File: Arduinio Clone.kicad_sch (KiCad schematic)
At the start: 0 parts

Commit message: Added child connectors schematic and symbols
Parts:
- added BT?: Battery, symbol Device:Battery
- added C?: C_Polarized, symbol Device:C_Polarized
- added C? (x2): C, symbol Device:C
- added D?: LED, symbol Device:LED
- added R? (x2): R, symbol Device:R
- added U?: 24LC1025, symbol Memory_EEPROM:24LC1025
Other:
- added sheet Connectors (Connectors.kicad_sch)
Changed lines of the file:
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@@
     (comment 1 "Designe by Giddie")
+  )
+  (symbol (lib_id "Device:LED") (at 93.98 90.17 0) (unit 1)
+    (in_bom yes) (on_board yes) (fields_autoplaced)
+    (property "Reference" "D?" (id 0) (at 92.3925 83.82 0))
+    (property "Value" "LED" (id 1) (at 92.3925 86.36 0))
+    (property "Footprint" "" (id 2) (at 93.98 90.17 0)
+      (effects (font (size 1.27 1.27)) hide)
+    )
+    (property "Datasheet" "~" (id 3) (at 93.98 90.17 0)
+      (effects (font (size 1.27 1.27)) hide)
+    )
+    (pin "1")
+    (pin "2")
+  )
+  (symbol (lib_id "Memory_EEPROM:24LC1025") (at 144.78 82.55 0) (unit 1)
+    (in_bom yes) (on_board yes) (fields_autoplaced)
+    (property "Reference" "U?" (id 0) (at 146.7994 72.39 0)
+      (effects (font (size 1.27 1.27)) (justify left))
+    )
+    (property "Value" "24LC1025" (id 1) (at 146.7994 74.93 0)
+      (effects (font (size 1.27 1.27)) (justify left))
+    )
+    (property "Footprint" "" (id 2) (at 144.78 82.55 0)
+      (effects (font (size 1.27 1.27)) hide)
+    )
+    (property "Datasheet" "http://ww1.microchip.com/downloads/en/DeviceDoc/21941B.pdf" (id 3) (at 144.78 82.55 0)
+      (effects (font (size 1.27 1.27)) hide)
+    )
+    (pin "1")
+    (pin "2")
+    (pin "3")
+    (pin "4")
+    (pin "5")
+    (pin "6")
+    (pin "7")
+    (pin "8")
+  )
+  (symbol (lib_id "Device:C_Polarized") (at 128.27 54.61 0) (unit 1)
+    (in_bom yes) (on_board yes) (fields_autoplaced)
+    (property "Reference" "C?" (id 0) (at 132.08 52.4509 0)
+      (effects (font (size 1.27 1.27)) (justify left))
+    )
+    (property "Value" "C_Polarized" (id 1) (at 132.08 54.9909 0)
+      (effects (font (size 1.27 1.27)) (justify left))
+    )
+    (property "Footprint" "" (id 2) (at 129.2352 58.42 0)
+      (effects (font (size 1.27 1.27)) hide)
+    )
+    (property "Datasheet" "~" (id 3) (at 128.27 54.61 0)
+      (effects (font (size 1.27 1.27)) hide)
+    )
+    (pin "1")
+    (pin "2")
+  )
+  (symbol (lib_id "Device:C") (at 91.44 55.88 0) (unit 1)
+    (in_bom yes) (on_board yes) (fields_autoplaced)
+    (property "Reference" "C?" (id 0) (at 95.25 54.6099 0)
+      (effects (font (size 1.27 1.27)) (justify left))
+    )
+    (property "Value" "C" (id 1) (at 95.25 57.1499 0)
+      (effects (font (size 1.27 1.27)) (justify left))
+    )
+    (property "Footprint" "" (id 2) (at 92.4052 59.69 0)
+      (effects (font (size 1.27 1.27)) hide)
+    )
+    (property "Datasheet" "~" (id 3) (at 91.44 55.88 0)
+      (effects (font (size 1.27 1.27)) hide)
+    )
+    (pin "1")
+    (pin "2")
+  )
+  (symbol (lib_id "Device:R") (at 123.19 87.63 0) (unit 1)
+    (in_bom yes) (on_board yes) (fields_autoplaced)
+    (property "Reference" "R?" (id 0) (at 125.73 86.3599 0)
+      (effects (font (size 1.27 1.27)) (justify left))
+    )
+    (property "Value" "R" (id 1) (at 125.73 88.8999 0)
+      (effects (font (size 1.27 1.27)) (justify left))
+    )
+    (property "Footprint" "" (id 2) (at 121.412 87.63 90)
+      (effects (font (size 1.27 1.27)) hide)
+    )
+    (property "Datasheet" "~" (id 3) (at 123.19 87.63 0)
+      (effects (font (size 1.27 1.27)) hide)
+    )
+    (pin "1")
+    (pin "2")
+  )
+  (symbol (lib_id "Device:Battery") (at 63.5 53.34 0) (unit 1)
+    (in_bom yes) (on_board yes) (fields_autoplaced)
+    (property "Reference" "BT?" (id 0) (at 67.31 51.6889 0)
+      (effects (font (size 1.27 1.27)) (justify left))
+    )
+    (property "Value" "Battery" (id 1) (at 67.31 54.2289 0)
+      (effects (font (size 1.27 1.27)) (justify left))
+    )
+    (property "Footprint" "" (id 2) (at 63.5 51.816 90)
+      (effects (font (size 1.27 1.27)) hide)
+    )
+    (property "Datasheet" "~" (id 3) (at 63.5 51.816 90)
+      (effects (font (size 1.27 1.27)) hide)
+    )
+    (pin "1")
+    (pin "2")
+  )
+  (symbol (lib_id "Device:R") (at 111.76 71.12 0) (unit 1)
+    (in_bom yes) (on_board yes) (fields_autoplaced)
+    (property "Reference" "R?" (id 0) (at 114.3 69.8499 0)
+      (effects (font (size 1.27 1.27)) (justify left))
+    )
+    (property "Value" "R" (id 1) (at 114.3 72.3899 0)
+      (effects (font (size 1.27 1.27)) (justify left))
+    )
+    (property "Footprint" "" (id 2) (at 109.982 71.12 90)
+      (effects (font (size 1.27 1.27)) hide)
+    )
+    (property "Datasheet" "~" (id 3) (at 111.76 71.12 0)
+      (effects (font (size 1.27 1.27)) hide)
+    )
+    (pin "1")
+    (pin "2")
+  )
+  (symbol (lib_id "Device:C") (at 110.49 53.34 0) (unit 1)
+    (in_bom yes) (on_board yes) (fields_autoplaced)
+    (property "Reference" "C?" (id 0) (at 114.3 52.0699 0)
+      (effects (font (size 1.27 1.27)) (justify left))
+    )
+    (property "Value" "C" (id 1) (at 114.3 54.6099 0)
+      (effects (font (size 1.27 1.27)) (justify left))
+    )
+    (property "Footprint" "" (id 2) (at 111.4552 57.15 0)
+      (effects (font (size 1.27 1.27)) hide)
+    )
+    (property "Datasheet" "~" (id 3) (at 110.49 53.34 0)
+      (effects (font (size 1.27 1.27)) hide)
+    )
+    (pin "1")
+    (pin "2")
+  )
+  (sheet (at 68.58 110.49) (size 57.15 49.53) (fields_autoplaced)
+    (stroke (width 0.1524) (type solid) (color 0 0 0 0))
+    (fill (color 0 0 0 0.0000))
+    (property "Sheet name" "Connectors" (id 0) (at 68.58 109.7784 0)
+      (effects (font (size 1.27 1.27)) (justify left bottom))
+    )
+    (property "Sheet file" "Connectors.kicad_sch" (id 1) (at 68.58 160.6046 0)
+      (effects (font (size 1.27 1.27)) (justify left top))
+    )
   )
   (sheet_instances
     (path "/" (page "1"))
+    (path "/99dcd93f-6742-4b81-a071-043df0a32b88" (page "2"))
+  )
+  (symbol_instances
+    (path "/cb99d522-d98f-4f2e-af24-39a642a2262c"
+      (reference "BT?") (unit 1) (value "Battery") (footprint "")
+    )
+    (path "/47ac9772-3d12-4e4c-be34-49c86c4d11b8"
+      (reference "C?") (unit 1) (value "C_Polarized") (footprint "")
+    )
+    (path "/a0a7411e-2ace-431e-9190-e1efd84cfa19"
+      (reference "C?") (unit 1) (value "C") (footprint "")
+    )
+    (path "/f4cd744f-86c3-401e-9dc4-f3966535b983"
+      (reference "C?") (unit 1) (value "C") (footprint "")
+    )
+    (path "/10f0ad0a-5347-4cd8-9e8b-b551768717e1"
+      (reference "D?") (unit 1) (value "LED") (footprint "")
+    )
+    (path "/99dcd93f-6742-4b81-a071-043df0a32b88/627a6bb9-dcd8-4955-91b8-8ac1c7ba0267"
+      (reference "J?") (unit 1) (value "Conn_01x09") (footprint "")
+    )
+    (path "/99dcd93f-6742-4b81-a071-043df0a32b88/70a1e371-96bd-43fc-8ac7-1645345d3e46"
+      (reference "J?") (unit 1) (value "Conn_02x03_Odd_Even") (footprint "")
+    )
+    (path "/99dcd93f-6742-4b81-a071-043df0a32b88/b8095f78-b7cb-4edb-8f3b-82dfbdf61388"
+      (reference "J?") (unit 1) (value "Conn_01x04") (footprint "")
+    )
+    (path "/99dcd93f-6742-4b81-a071-043df0a32b88/dd61ea61-ee00-483a-9cf3-44579a861992"
+      (reference "J?") (unit 1) (value "Conn_01x04") (footprint "")
+    )
+    (path "/a514a1f9-319e-4854-bd4a-fb2006c92301"
+      (reference "R?") (unit 1) (value "R") (footprint "")
+    )
+    (path "/e1e0cd89-7085-4b67-b9fa-c00a933b2bea"
+      (reference "R?") (unit 1) (value "R") (footprint "")
+    )
+    (path "/243ad795-d45f-41d7-b66a-04b2d1180b1c"
+      (reference "U?") (unit 1) (value "24LC1025") (footprint "")
+    )
   )
 )

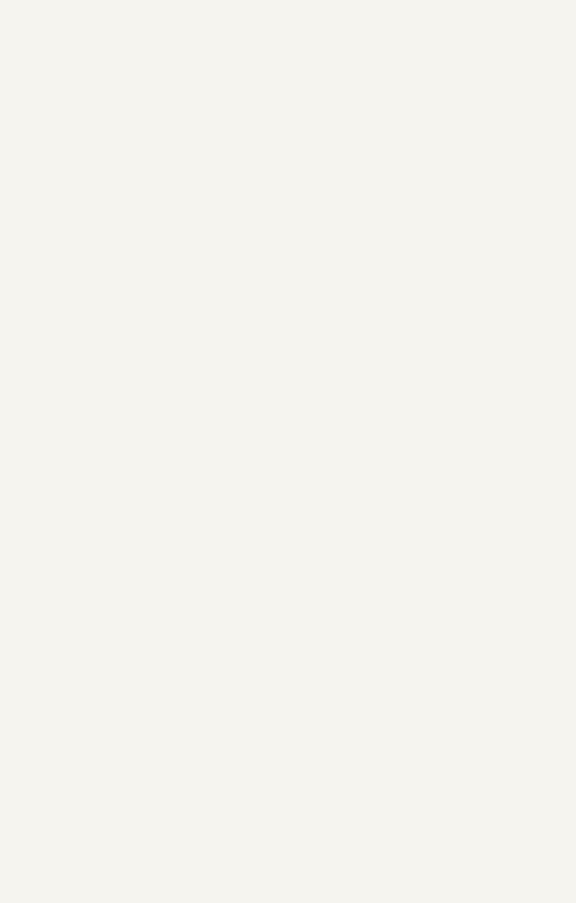
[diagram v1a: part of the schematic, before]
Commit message: Added Atmega328p-A symbol
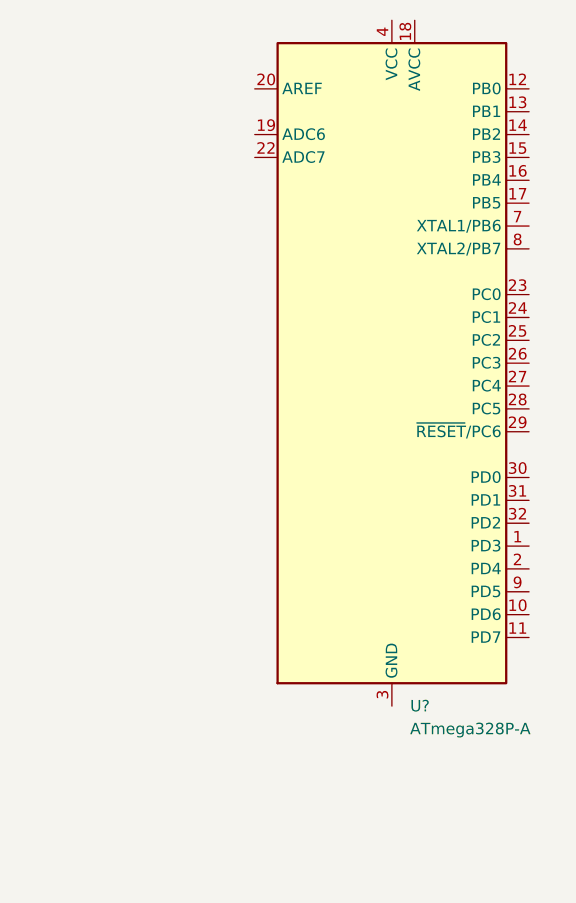
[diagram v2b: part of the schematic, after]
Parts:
- added U?: ATmega328P-A, Package_QFP:TQFP-32_7x7mm_P0.8mm, symbol MCU_Microchip_ATmega:ATmega328P-A
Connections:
- new net: U?.21 (GND), U?.3 (GND), U?.5 (GND)
- new net: U?.4 (VCC), U?.6 (VCC)
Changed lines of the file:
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@@
     (pin "2")
+  )
+  (symbol (lib_id "MCU_Microchip_ATmega:ATmega328P-A") (at 208.28 78.74 0) (unit 1)
+    (in_bom yes) (on_board yes) (fields_autoplaced)
+    (property "Reference" "U?" (id 0) (at 210.2994 116.84 0)
+      (effects (font (size 1.27 1.27)) (justify left))
+    )
+    (property "Value" "ATmega328P-A" (id 1) (at 210.2994 119.38 0)
+      (effects (font (size 1.27 1.27)) (justify left))
+    )
+    (property "Footprint" "Package_QFP:TQFP-32_7x7mm_P0.8mm" (id 2) (at 208.28 78.74 0)
+      (effects (font (size 1.27 1.27) italic) hide)
+    )
+    (property "Datasheet" "http://ww1.microchip.com/downloads/en/DeviceDoc/ATmega328_P%20AVR%20MCU%20with%20picoPower%20Technology%20Data%20Sheet%2040001984A.pdf" (id 3) (at 208.28 78.74 0)
+      (effects (font (size 1.27 1.27)) hide)
+    )
+    (pin "1")
+    (pin "10")
+    (pin "11")
+    (pin "12")
+    (pin "13")
+    (pin "14")
+    (pin "15")
+    (pin "16")
+    (pin "17")
+    (pin "18")
+    (pin "19")
+    (pin "2")
+    (pin "20")
+    (pin "21")
+    (pin "22")
+    (pin "23")
+    (pin "24")
+    (pin "25")
+    (pin "26")
+    (pin "27")
+    (pin "28")
+    (pin "29")
+    (pin "3")
+    (pin "30")
+    (pin "31")
+    (pin "32")
+    (pin "4")
+    (pin "5")
+    (pin "6")
+    (pin "7")
+    (pin "8")
+    (pin "9")
   )
   (symbol (lib_id "Device:C") (at 91.44 55.88 0) (unit 1)
@@
       (reference "U?") (unit 1) (value "24LC1025") (footprint "")
     )
+    (path "/7f29ecb0-6265-4d60-8278-7704387a2057"
+      (reference "U?") (unit 1) (value "ATmega328P-A") (footprint "Package_QFP:TQFP-32_7x7mm_P0.8mm")
+    )
   )

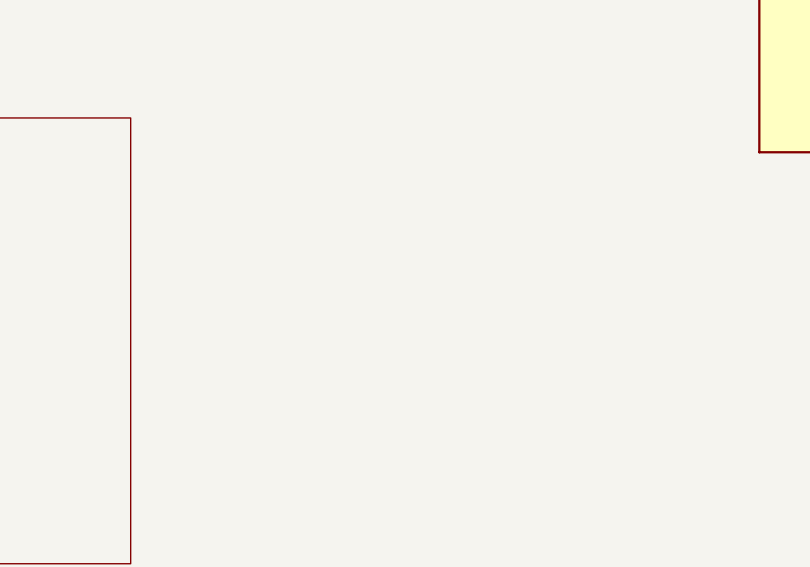
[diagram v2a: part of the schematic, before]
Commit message: Added custom DS1337 RTC symbol
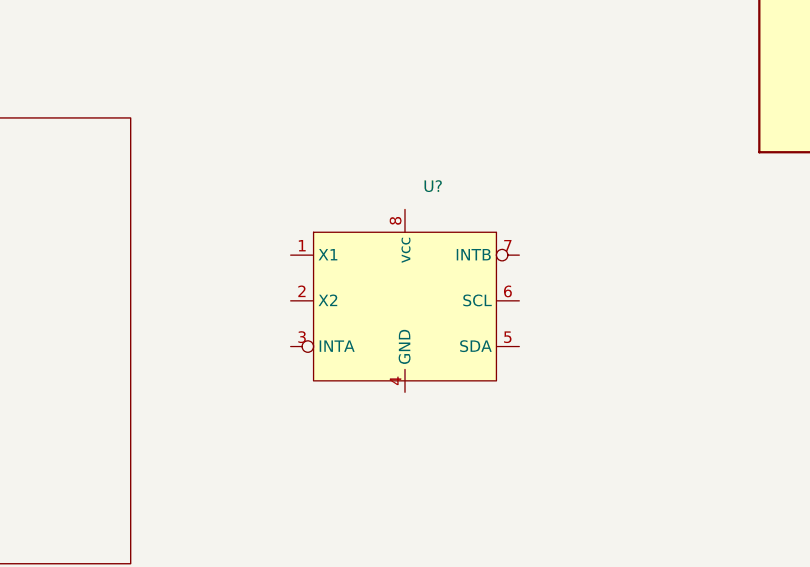
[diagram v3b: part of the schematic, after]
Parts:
- added U?: (no value), symbol GM_LIbrary:DS1337_GM
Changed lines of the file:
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@@
     (pin "2")
+  )
+  (symbol (lib_id "GM_LIbrary:DS1337_GM") (at 156.21 130.81 0) (unit 1)
+    (in_bom yes) (on_board yes) (fields_autoplaced)
+    (property "Reference" "U?" (id 0) (at 158.2294 118.11 0)
+      (effects (font (size 1.27 1.27)) (justify left))
+    )
+    (property "Value" "" (id 1) (at 158.2294 120.65 0)
+      (effects (font (size 1.27 1.27)) (justify left))
+    )
+    (property "Footprint" "" (id 2) (at 156.21 129.54 0)
+      (effects (font (size 1.27 1.27)) hide)
+    )
+    (property "Datasheet" "https://datasheets.maximintegrated.com/en/ds/DS1337-DS1337C.pdf" (id 3) (at 160.02 146.05 0)
+      (effects (font (size 1.27 1.27)) hide)
+    )
+    (pin "1")
+    (pin "2")
+    (pin "3")
+    (pin "4")
+    (pin "5")
+    (pin "6")
+    (pin "7")
+    (pin "8")
   )
   (symbol (lib_id "MCU_Microchip_ATmega:ATmega328P-A") (at 208.28 78.74 0) (unit 1)
@@
       (reference "U?") (unit 1) (value "24LC1025") (footprint "")
     )
+    (path "/5184beda-4204-4a1a-836c-6ca14ccda6ee"
+      (reference "U?") (unit 1) (value "DS1337_GM") (footprint "")
+    )
     (path "/7f29ecb0-6265-4d60-8278-7704387a2057"

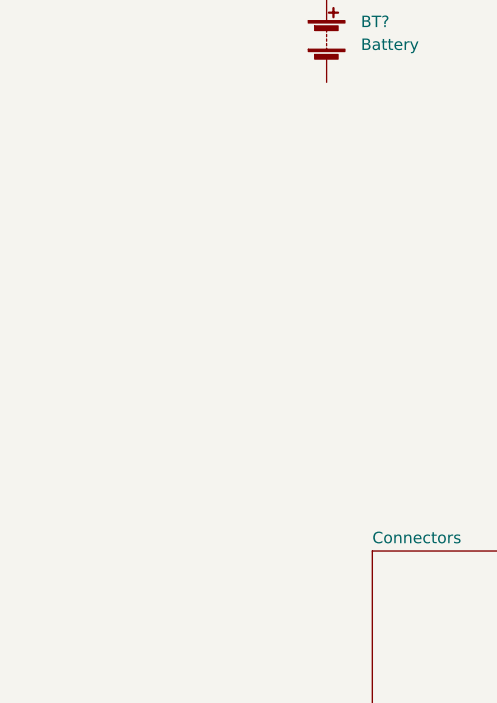
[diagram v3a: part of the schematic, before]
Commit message: Added crystals to schematic
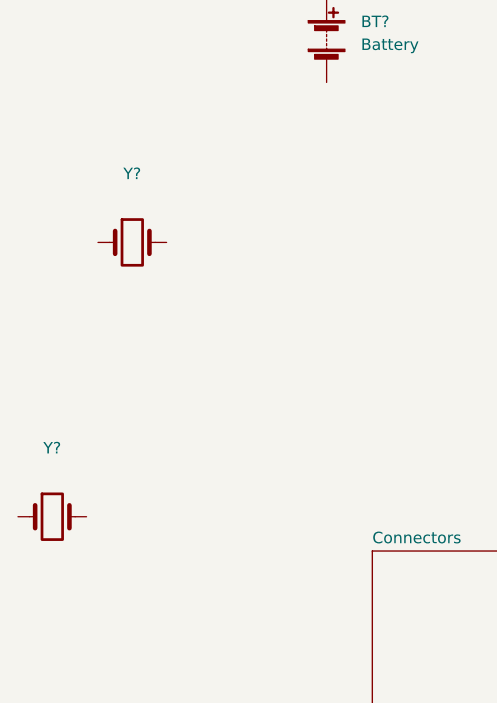
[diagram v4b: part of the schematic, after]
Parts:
- added Y? (x2): (no value), symbol Device:Crystal
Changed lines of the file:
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@@
     (pin "8")
+  )
+  (symbol (lib_id "Device:Crystal") (at 41.91 76.2 0) (unit 1)
+    (in_bom yes) (on_board yes) (fields_autoplaced)
+    (property "Reference" "Y?" (id 0) (at 41.91 68.58 0))
+    (property "Value" "" (id 1) (at 41.91 71.12 0))
+    (property "Footprint" "" (id 2) (at 41.91 76.2 0)
+      (effects (font (size 1.27 1.27)) hide)
+    )
+    (property "Datasheet" "~" (id 3) (at 41.91 76.2 0)
+      (effects (font (size 1.27 1.27)) hide)
+    )
+    (pin "1")
+    (pin "2")
   )
   (symbol (lib_id "Device:C_Polarized") (at 128.27 54.61 0) (unit 1)
@@
     (pin "2")
   )
+  (symbol (lib_id "Device:Crystal") (at 33.02 106.68 0) (unit 1)
+    (in_bom yes) (on_board yes) (fields_autoplaced)
+    (property "Reference" "Y?" (id 0) (at 33.02 99.06 0))
+    (property "Value" "" (id 1) (at 33.02 101.6 0))
+    (property "Footprint" "" (id 2) (at 33.02 106.68 0)
+      (effects (font (size 1.27 1.27)) hide)
+    )
+    (property "Datasheet" "~" (id 3) (at 33.02 106.68 0)
+      (effects (font (size 1.27 1.27)) hide)
+    )
+    (pin "1")
+    (pin "2")
+  )
   (symbol (lib_id "Device:R") (at 111.76 71.12 0) (unit 1)
     (in_bom yes) (on_board yes) (fields_autoplaced)
@@
       (reference "U?") (unit 1) (value "ATmega328P-A") (footprint "Package_QFP:TQFP-32_7x7mm_P0.8mm")
     )
-  )
+    (path "/3fb113a1-a012-4b2e-a31d-61ea5b0c93b6"
+      (reference "Y?") (unit 1) (value "Crystal") (footprint "")
+    )
+    (path "/d8dd4a5f-dc16-4ac5-8b31-704bbe349563"
+      (reference "Y?") (unit 1) (value "Crystal") (footprint "")
+    )
+  )

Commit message: Annotation
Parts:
- U1: renamed from U?; value (none) -> DS1337_GM
- Y1, Y2: renamed from Y?; value (none) -> Crystal
- gave numbers to parts that had none: 9
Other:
- moved on the sheet: BT1, C2, C3, D1, R1, R2, U1, U2, U3, Y1, Y2
